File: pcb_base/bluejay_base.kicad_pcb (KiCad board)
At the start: 2 copper layers, 147 x 140.5 mm, 9 parts

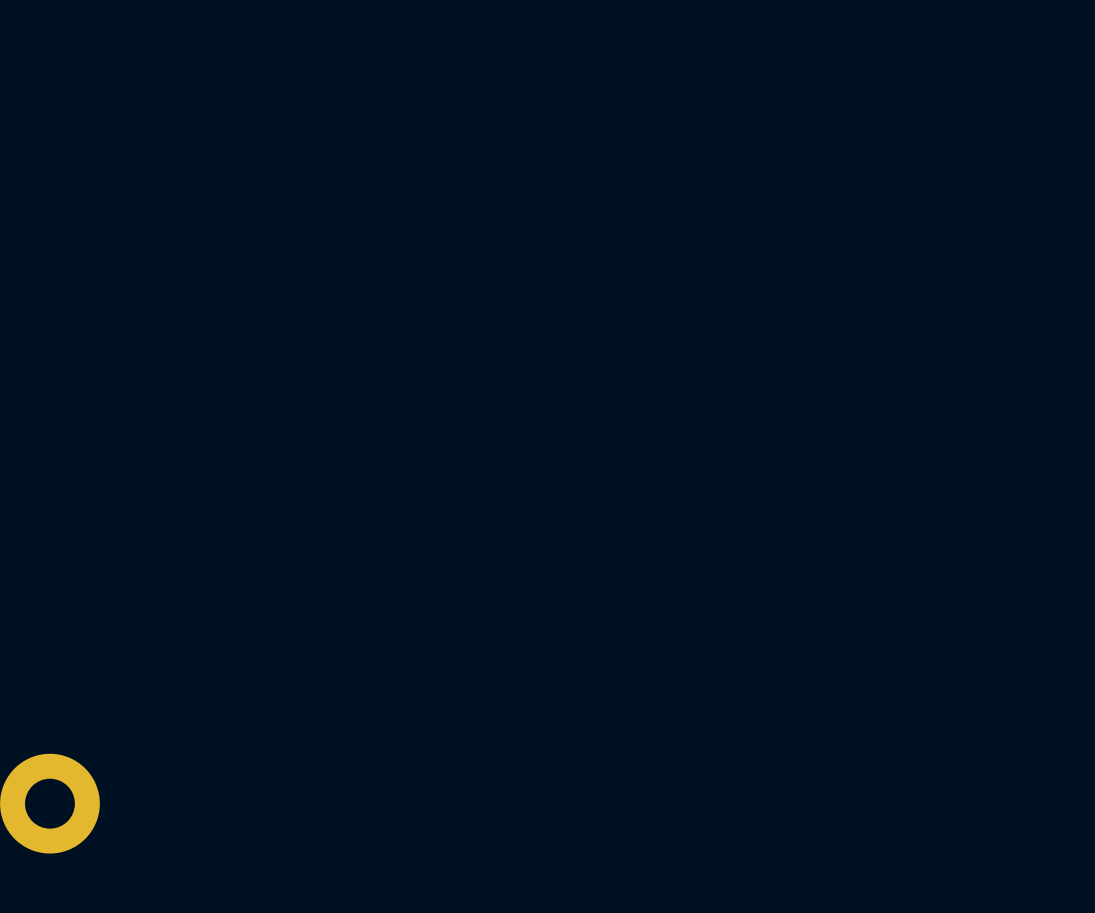
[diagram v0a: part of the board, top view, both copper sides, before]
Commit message: add logo
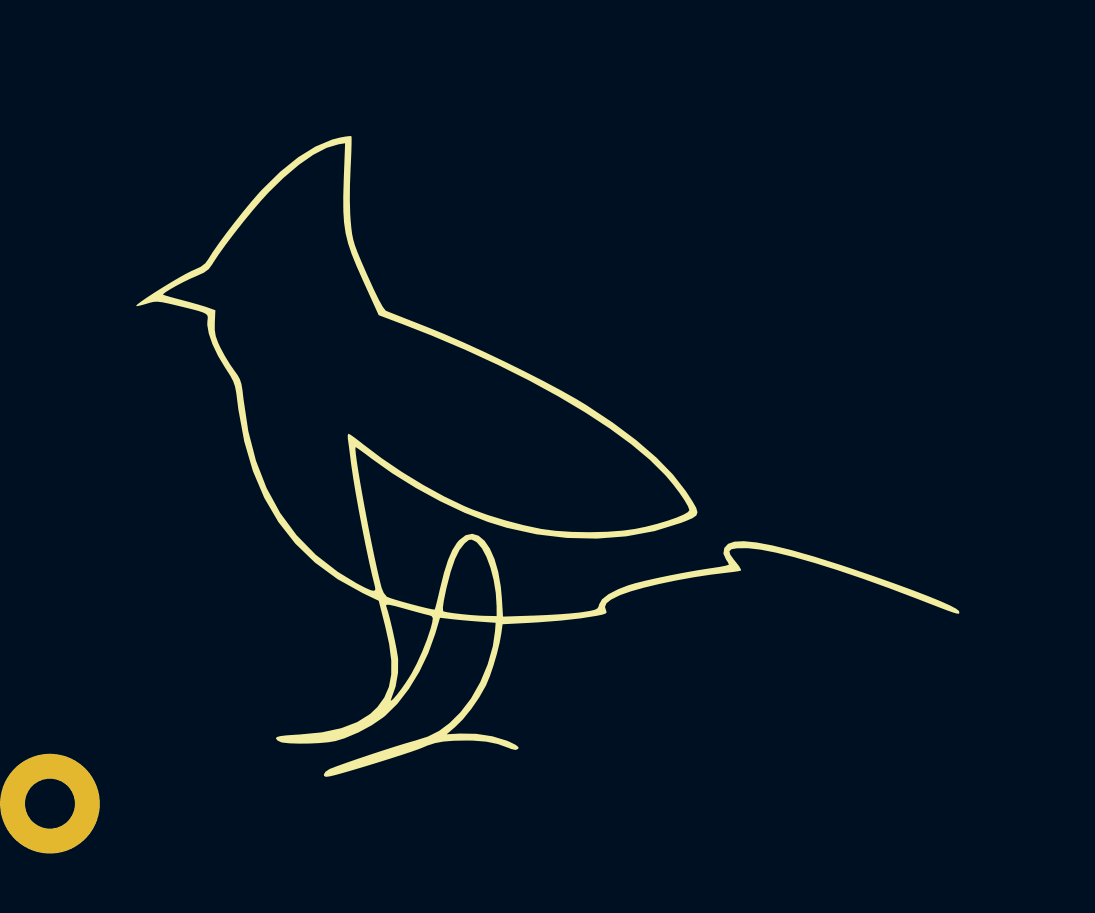
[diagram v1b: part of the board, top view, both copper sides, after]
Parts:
- added G***: LOGO, BlueJay footprints:bluejay_logo, F.Cu at (-7.25, -5.75)
- added G***: LOGO, BlueJay footprints:bluejay_logo, B.Cu at (-7.25, -5.75)

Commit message: work on plate
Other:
- board text added: "JLCJLCJLCJLC"
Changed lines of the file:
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@@
   (gr_line (start 57.05 -56.4) (end -84.024489 -56.3437) (layer "Edge.Cuts") (width 0.1))
   (gr_arc (start 49.7812 83.7263) (mid 48.888799 84.147698) (end 48.0112 83.6963) (layer "Edge.Cuts") (width 0.1))
+  (gr_text "JLCJLCJLCJLC" (at -80.5 35.33) (layer "F.Cu")
+    (effects (font (size 1 1) (thickness 0.2)))
+  )
   (zone (net 1) (net_name "GND") (layers F&B.Cu) (hatch edge 0.508)
     (connect_pads (clearance 0.508))

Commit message: Fine tune pcbs
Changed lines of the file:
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@@
   (gr_line (start 57.05 -56.4) (end -84.024489 -56.3437) (layer "Edge.Cuts") (width 0.1))
   (gr_arc (start 49.7812 83.7263) (mid 48.888799 84.147698) (end 48.0112 83.6963) (layer "Edge.Cuts") (width 0.1))
-  (gr_text "JLCJLCJLCJLC" (at -80.5 35.33) (layer "F.Cu")
+  (gr_text "JLCJLCJLCJLC" (at -80.5 35.33) (layer "F.SilkS")
     (effects (font (size 1 1) (thickness 0.2)))
   )
@@
     (connect_pads (clearance 0.508))
     (min_thickness 0.254) (filled_areas_thickness no)
-    (fill yes (thermal_gap 0.508) (thermal_bridge_width 0.508) (island_removal_mode 1) (island_area_min 0))
+    (fill yes (thermal_gap 0.508) (thermal_bridge_width 0.508))
     (polygon
       (pts

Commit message: Produce test gerber files
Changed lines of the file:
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@@
     )
     (pad_to_mask_clearance 0)
-    (solder_mask_min_width 0.12)
     (pcbplotparams
-      (layerselection 0x00010fc_ffffffff)
+      (layerselection 0x00010f0_ffffffff)
       (disableapertmacros false)
       (usegerberextensions false)
@@
       (outputformat 1)
       (mirror false)
-      (drillshape 1)
+      (drillshape 0)
       (scaleselection 1)
-      (outputdirectory "")
+      (outputdirectory "../gerber/")
     )
   )
@@
   (gr_arc (start 49.7812 83.7263) (mid 48.888799 84.147698) (end 48.0112 83.6963) (layer "Edge.Cuts") (width 0.1))
   (gr_text "JLCJLCJLCJLC" (at -80.5 35.33) (layer "F.SilkS")
-    (effects (font (size 1 1) (thickness 0.2)))
+    (effects (font (size 1 1) (thickness 0.15)))
   )
   (zone (net 1) (net_name "GND") (layers F&B.Cu) (hatch edge 0.508)

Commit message: Update schematics in preparation for review
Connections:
- net GND renamed Earth
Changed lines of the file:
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@@
   )
   (net 0 "")
-  (net 1 "GND")
+  (net 1 "Earth")
   (footprint "MountingHole:MountingHole_2.2mm_M2_Pad" (layer "F.Cu")
     (at 56.95 64.15)
@@
     (fp_circle (center 0 0) (end 2.45 0) (layer "F.CrtYd") (width 0.05) (fill none))
     (pad "1" thru_hole circle (at 0 0) (size 4.4 4.4) (drill 2.2) (layers *.Cu *.Mask)
-      (net 1 "GND") (pinfunction "1") (pintype "input"))
+      (net 1 "Earth") (pinfunction "1") (pintype "input"))
   )
   (footprint "MountingHole:MountingHole_2.2mm_M2_Pad" (layer "F.Cu")
@@
     (effects (font (size 1 1) (thickness 0.15)))
   )
-  (zone (net 1) (net_name "GND") (layers F&B.Cu) (hatch edge 0.508)
+  (zone (net 1) (net_name "Earth") (layers F&B.Cu) (hatch edge 0.508)
     (connect_pads (clearance 0.508))
     (min_thickness 0.254) (filled_areas_thickness no)

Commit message: Fine tuning of schematics and pcbs in prep for review
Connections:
- net Earth renamed GND
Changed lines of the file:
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@@
   )
   (net 0 "")
-  (net 1 "Earth")
+  (net 1 "GND")
   (footprint "MountingHole:MountingHole_2.2mm_M2_Pad" (layer "F.Cu")
     (at 56.95 64.15)
@@
     (fp_circle (center 0 0) (end 2.45 0) (layer "F.CrtYd") (width 0.05) (fill none))
     (pad "1" thru_hole circle (at 0 0) (size 4.4 4.4) (drill 2.2) (layers *.Cu *.Mask)
-      (net 1 "Earth") (pinfunction "1") (pintype "input"))
+      (net 1 "GND") (pinfunction "1") (pintype "input"))
   )
   (footprint "MountingHole:MountingHole_2.2mm_M2_Pad" (layer "F.Cu")
@@
     (effects (font (size 1 1) (thickness 0.15)))
   )
-  (zone (net 1) (net_name "Earth") (layers F&B.Cu) (hatch edge 0.508)
+  (zone (net 1) (net_name "GND") (layers F&B.Cu) (hatch edge 0.508)
     (connect_pads (clearance 0.508))
     (min_thickness 0.254) (filled_areas_thickness no)

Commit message: Update logo
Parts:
- G*** (x2): footprint BlueJay footprints:bluejay_logo -> BlueJay footprints:BlueJay_Logo_New_Large
- moved G*** 16.4 mm to (-21.7, -13.5) (x2)

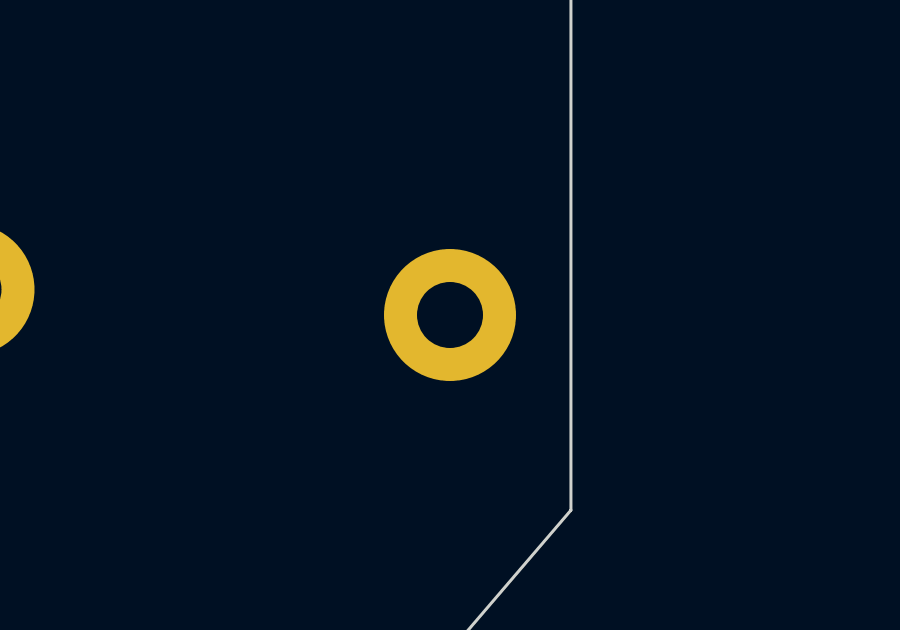
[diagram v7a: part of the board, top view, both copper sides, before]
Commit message: remove mounting hole 9
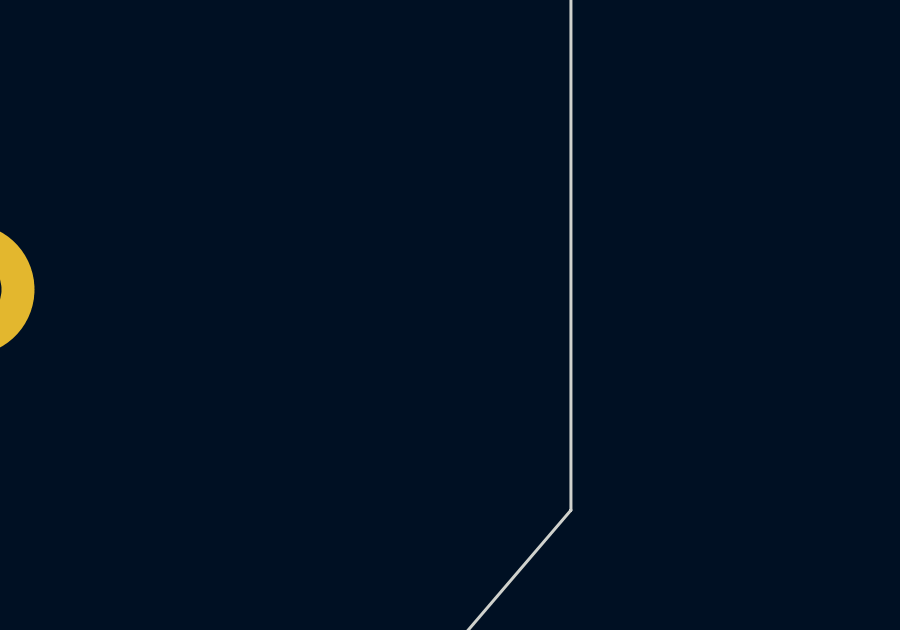
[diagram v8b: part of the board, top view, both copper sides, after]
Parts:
- removed H9: M2, MountingHole:MountingHole_2.2mm_M2_Pad
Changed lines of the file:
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@@
   (net 1 "GND")
-  (footprint "MountingHole:MountingHole_2.2mm_M2_Pad" (layer "F.Cu")
-    (at 56.95 64.15)
-    (descr "Mounting Hole 2.2mm, M2")
-    (tags "mounting hole 2.2mm m2")
-    (property "Sheetfile" "bluejay_base.kicad_sch")
-    (property "Sheetname" "")
-    (property "exclude_from_bom" "")
-    (attr exclude_from_pos_files exclude_from_bom)
-    (fp_text reference "H9" (at 0 -3.2) (layer "F.Fab")
-      (effects (font (size 1 1) (thickness 0.15)))
-    )
-    (fp_text value "M2" (at 0 3.2) (layer "F.Fab")
-      (effects (font (size 1 1) (thickness 0.15)))
-    )
-    (fp_text user "${REFERENCE}" (at 0 0) (layer "F.Fab")
-      (effects (font (size 1 1) (thickness 0.15)))
-    )
-    (fp_circle (center 0 0) (end 2.2 0) (layer "Cmts.User") (width 0.15) (fill none))
-    (fp_circle (center 0 0) (end 2.45 0) (layer "F.CrtYd") (width 0.05) (fill none))
-    (pad "1" thru_hole circle (at 0 0) (size 4.4 4.4) (drill 2.2) (layers *.Cu *.Mask))
-  )
   (footprint "MountingHole:MountingHole_2.2mm_M2_Pad" (layer "F.Cu")
     (at 40.9 63.3)
